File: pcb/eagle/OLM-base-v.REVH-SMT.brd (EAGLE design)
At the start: 91.9 x 57.4 mm, 55 parts, among them CN1 MiniB USB, IC1 LP2985-3.3v, IC2 ATMEGA32U4-AU, IC3 DS1307, IC4 ENC28J60, T1 IRLML2246, U1 USD-SOCKETMICRO-SD-SOCKET-TAO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, X1 8MHz, X2 32.657k, X2A 25MHz, X2A1 25MHz

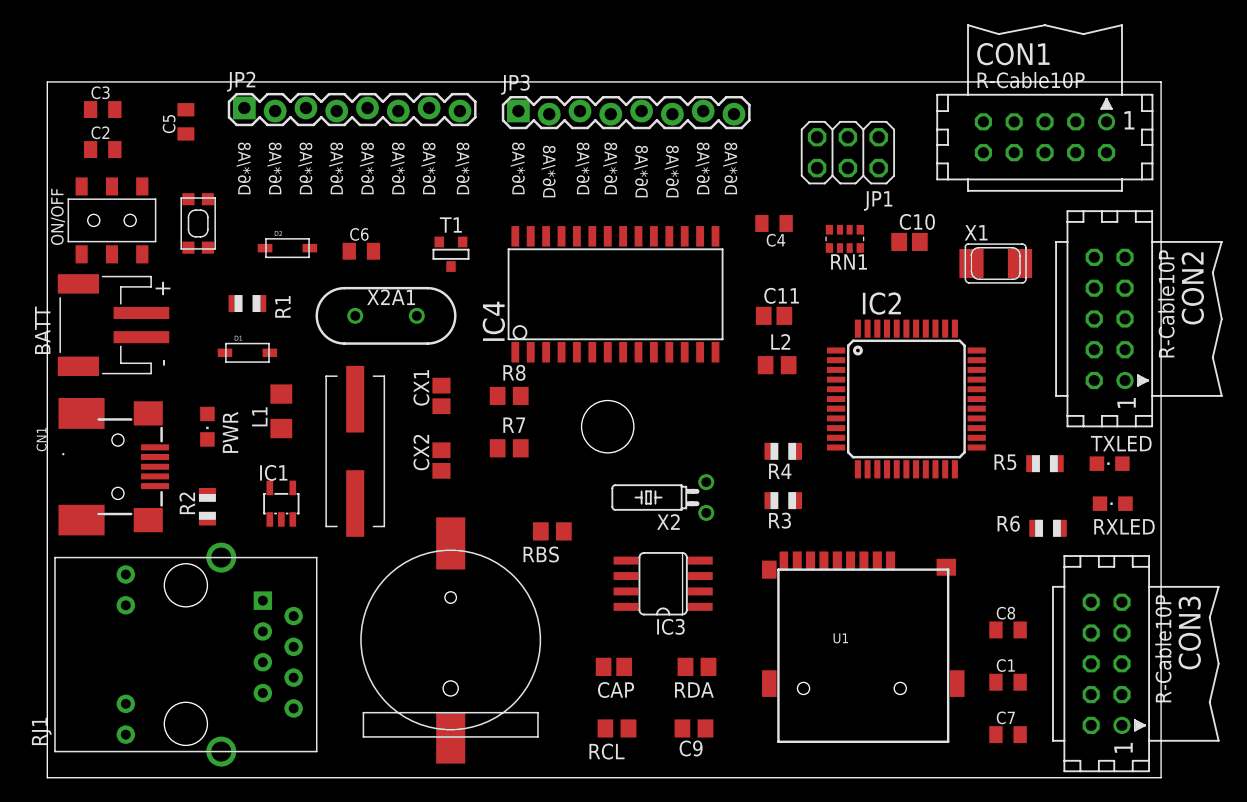
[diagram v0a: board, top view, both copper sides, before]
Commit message: rewired surface mount version
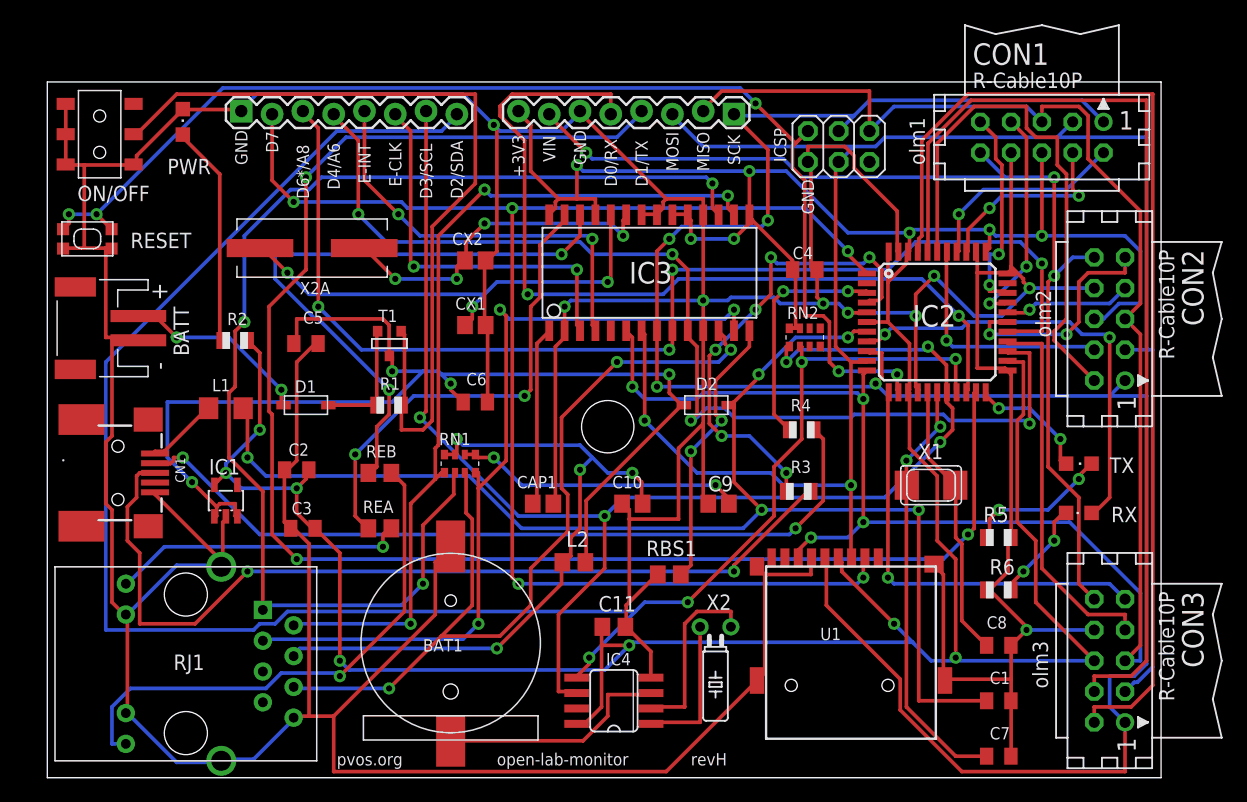
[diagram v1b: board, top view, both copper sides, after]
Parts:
- removed CAP: 10u, resistor:C0805
- removed R7, R8: 330, rcl:R0805
- removed RBS: 2.32K, rcl:R0805
- removed RCL, RDA: 10K, rcl:R0805
- removed RXLED, TXLED: YELLOW, adafruit:CHIPLED_0805
- removed X2A1: 25MHz, SparkFun:HC49US
- added CAP1: 10u, resistor:C0805
- added RBS1: 2.32K, rcl:R0805
- added REA, REB: 330, rcl:R0805
- added RN2: (no value), resistor-dil:EXB38V
- added RX, TX: YELLOW, adafruit:CHIPLED_0805
- C11: value 0.1µ -> 0.1u; device resistor:C0805 -> rcl:C0805
- C9: value 0.1u -> 0.1µ; device rcl:C0805 -> resistor:C0805
- IC3: value DS1307 -> ENC28J60; device adafruit:SO08 -> SparkFun:SOIC28WLONG
- IC4: value ENC28J60 -> DS1307; device SparkFun:SOIC28WLONG -> adafruit:SO08
- X2: value 32.657k -> 32.768kHz
- moved C3 38.3 mm to (21.1, 20.6), turned to 180 degrees
- moved D2 36.9 mm to (54.4, 30.7)
- moved RN1 36.8 mm to (34.0, 25.9), turned to 0 degrees
- moved IC4 33.5 mm to (46.7, 6.35), turned to 90 degrees
- moved C10 31.4 mm to (48.3, 22.6)
- moved C2 30.9 mm to (20.6, 25.4), turned to 180 degrees
- moved C11 28.9 mm to (46.7, 12.4)
- moved IC3 25.7 mm to (50.3, 41.7), turned to 0 degrees
- moved PWR 25.2 mm to (11.2, 54.1), turned to 0 degrees
- moved L2 23.4 mm to (43.4, 17.8)
- moved C5 20.8 mm to (21.3, 35.8), turned to 0 degrees
- moved X1 19.1 mm to (72.9, 24.1)
- moved C9 18.7 mm to (55.4, 22.6)
- moved JP3 17.8 mm to (56.6, 54.9), turned to 180 degrees
- moved X2A 17.1 mm to (21.8, 43.7), turned to 180 degrees
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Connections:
- removed net MISO/D12: CON1.5, CON2.5, CON3.5
- removed net MOSI/D11: CON1.3, CON2.3, CON3.3
- removed net N$34: IC4.27, R7.1
- removed net N$36: BAT1.P$2, IC3.3
- removed net N$37: IC4.26, R8.1
- removed net N$39: CAP.1, IC4.1
- removed net N$41: CX1.1, IC4.24, X2A.P$2, X2A1.2
- removed net N$42: CX2.1, IC4.23, X2A.P$1, X2A1.1
- removed net N$47: IC3.1, X2.1
- removed net N$50: IC3.2, X2.2
- removed net N$54: C10.2, RN1.5, RN1.6
- removed net N$59: IC4.14, RBS.2
- removed net SCK/D13: CON1.1, CON2.1, CON3.1
- new net N$10: C9.2, RN1.5, RN1.6
- new net N$14: IC3.27, REA.1
- new net N$15: IC3.26, REB.1
- new net N$16: CAP1.1, IC3.1
- new net N$17: IC3.14, RBS1.2
- new net N$18: CX1.1, IC3.24, X2A.P$2
- new net N$19: CX2.1, IC3.23, X2A.P$1
- new net N$20: BAT1.P$2, IC4.3
- new net N$21: IC4.1, X2.2
- new net N$30: IC4.2, X2.1
- net +3V3: now also C11.1, IC3.15, IC3.19, IC3.20, IC3.25, IC3.28, IC4.8, JP3.8, RN2.7, RN2.8; no longer C9.1, IC3.8, IC4.15, IC4.19, IC4.20, IC4.25, IC4.28, RCL.1, RDA.1
- net D2/SDA: now also IC4.5, RN2.2; no longer IC3.5, RDA.2
- net D3/SCL: now also IC4.6, RN2.1; no longer IC3.6, RCL.2
- net D4/A6: now also IC3.10; no longer IC4.10
- net D6*/A8: now also IC3.9; no longer IC4.9
- net E-CLK: now also IC3.3; no longer IC4.3
- net E-INT: now also IC3.4; no longer IC4.4
- net GND: now also C11.2, C9.1, CAP1.2, IC3.11, IC3.18, IC3.2, IC3.21, IC3.22, IC4.4, RBS1.1, U1.GND1, U1.GND3, U1.P$1, U1.P$2; no longer C11.1, C9.2, CAP.2, IC3.4, IC4.11, IC4.18, IC4.2, IC4.21, IC4.22, RBS.1
- net LEDA: now also REA.2; no longer R7.2
- net LEDB: now also REB.2; no longer R8.2
- net MISO: now also CON1.5, CON2.5, CON3.5, IC3.6; no longer IC4.6
- net MOSI: now also CON1.3, CON2.3, CON3.3, IC3.7; no longer IC4.7
- net N$11: now also TX.C; no longer TXLED.C
- net N$12: now also RX.C; no longer RXLED.C
- net RD+: now also IC3.13; no longer IC4.13
- net RD-: now also IC3.12; no longer IC4.12
- net RXLED/SS: now also RX.A; no longer RXLED.A
- net SCK: now also CON1.1, CON2.1, CON3.1, IC3.8; no longer IC4.8
- net TCT: now also C10.2; no longer C11.2
- net TD+: now also IC3.17; no longer IC4.17
- net TD-: now also IC3.16; no longer IC4.16
- net TXLED: now also TX.A; no longer TXLED.A
- net VCC: no longer JP3.8
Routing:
- net GND: track 0.00 -> 542.2 mm, vias 0 -> 9
- net +3V3: track 0.00 -> 304.8 mm, vias 0 -> 14
- net SCK: track 0.00 -> 181.6 mm, vias 0 -> 4
- net MISO: track 0.00 -> 163.5 mm, vias 0 -> 4
- net D2/SDA: track 0.00 -> 156.7 mm, vias 0 -> 4
- net MOSI: track 0.00 -> 154.7 mm, vias 0 -> 2
- net D1/TX: track 0.00 -> 132.0 mm, vias 0 -> 3
- net D7/AIN0: track 0.00 -> 119.4 mm, vias 0 -> 5
- net D3/SCL: track 0.00 -> 114.8 mm, vias 0 -> 5
- net +5V: track 0.00 -> 108.5 mm, vias 0 -> 5
- net TD+: track 0.00 -> 100.6 mm, vias 0 -> 3
- net RST: track 0.00 -> 98.6 mm, vias 0 -> 5
- net VCC: track 0.00 -> 95.8 mm, vias 0 -> 4
- net D6*/A8: track 0.00 -> 94.4 mm, vias 0 -> 4
- net D4/A6: track 0.00 -> 88.0 mm, vias 0 -> 4
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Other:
- board text added: "+3V3"
- board text added: "BAT1"
- board text added: "D0/RX"
- board text added: "D1/TX"
- board text added: "D2/SDA"
- board text added: "D3/SCL"
- board text added: "D4/A6"
- board text added: "D7"
- board text added: "E-CLK"
- board text added: "E-INT"
- board text added: "GND"
- board text added: "ICSP"
- board text added: "MISO"
- board text added: "MOSI"
- board text added: "RESET"
- board text added: "SCK"
- board text added: "VIN"
- board text added: "X2A"
- board text added: "olm1"
- board text added: "olm2"
- board text added: "olm3"
- board text added: "open-lab-monitor"
- board text added: "pvos.org"
- board text added: "revH"

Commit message: fixed breakouts by adding reset pin
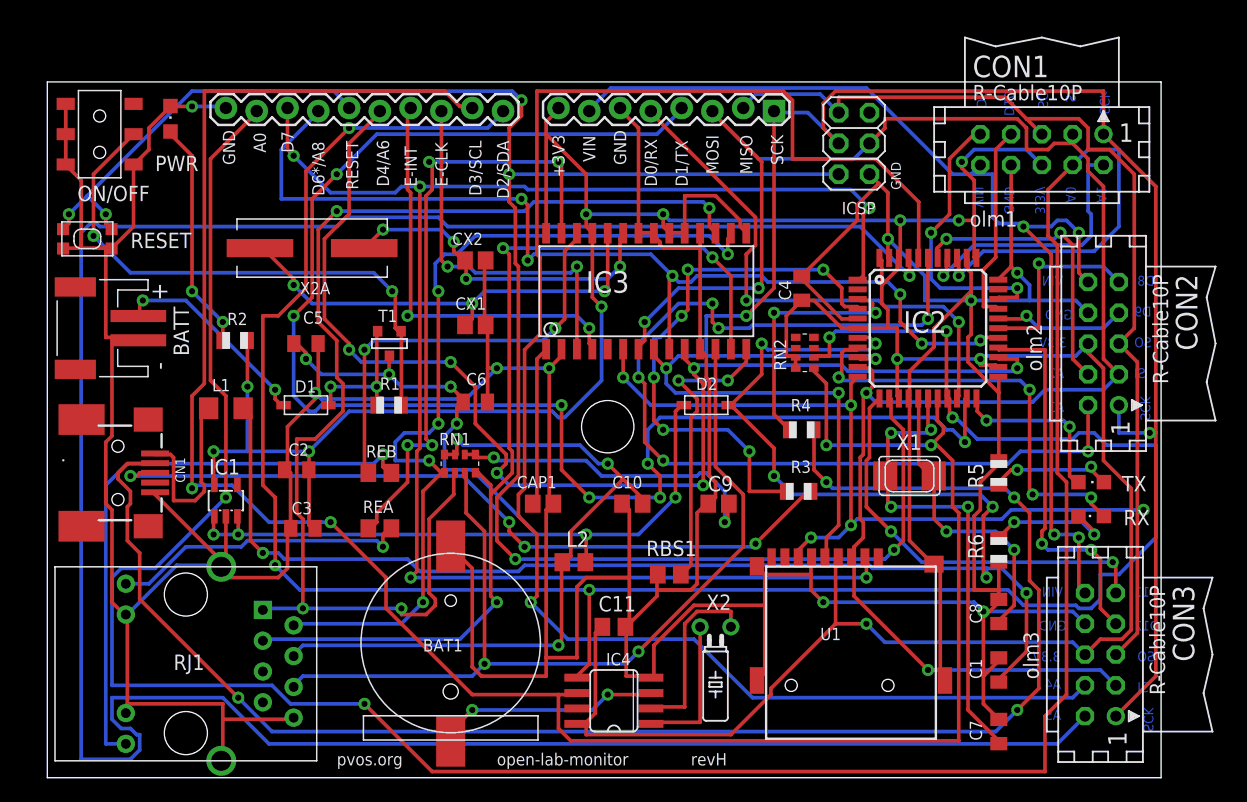
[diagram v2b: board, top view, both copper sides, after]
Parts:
- removed JP2: (no value), SparkFun-Connectors:1X08_LOCK
- added JP4: M10LOCK, SparkFun-Connectors:1X10_LOCK
- moved R5 5.33 mm to (78.5, 25.1), turned to 90 degrees
- moved JP3 3.31 mm to (59.9, 55.1)
- moved R6 3.30 mm to (78.5, 18.8), turned to 90 degrees
- moved C8 2.79 mm to (78.5, 13.7), turned to 90 degrees
- moved C1 2.54 mm to (78.5, 8.89), turned to 90 degrees
- moved CON2 2.09 mm to (87.1, 35.8)
- moved C7 2.03 mm to (78.5, 3.81), turned to 90 degrees
- moved X1 1.93 mm to (71.1, 24.9)
- moved TX 1.83 mm to (86.1, 24.4)
- moved IC3 1.55 mm to (50.0, 40.1)
- moved C4 1.55 mm to (62.2, 40.4), turned to 90 degrees
- moved JP1 1.30 mm to (66.5, 52.3), turned to 270 degrees
- moved RN2 1.27 mm to (62.5, 35.1), turned to 90 degrees
- moved PWR 1.05 mm to (10.2, 54.4)
- moved RX 1.05 mm to (86.1, 21.6)
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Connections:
- net A0: now also JP4.2
- net D2/SDA: now also JP4.10; no longer JP2.8
- net D3/SCL: now also JP4.9; no longer JP2.7
- net D4/A6: now also JP4.6; no longer JP2.4
- net D6*/A8: now also JP4.4; no longer JP2.3
- net D7/AIN0: now also JP4.3; no longer JP2.2
- net E-CLK: now also JP4.8; no longer JP2.6
- net E-INT: now also JP4.7; no longer JP2.5
- net GND: now also JP4.1; no longer JP2.1
- net RST: now also JP4.5
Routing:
- net A0: track 16.0 -> 214.3 mm, vias 2 -> 3
- net A5: track 85.6 -> 209.8 mm, vias 0 -> 1
- net N$5: track 65.5 -> 132.3 mm, vias 2 -> 4
- net D3/SCL: track 114.8 -> 178.1 mm, vias 5 -> 4
- net RST: track 98.6 -> 160.8 mm, vias 5 -> 6
- net A4: track 80.8 -> 136.0 mm, vias 0 -> 1
- net A3: track 44.4 -> 82.2 mm, vias 0 -> 6
- net GND: track 542.2 -> 508.0 mm
- net +5V: track 108.5 -> 137.0 mm, vias 5 -> 7
- net D2/SDA: track 156.7 -> 184.8 mm, vias 4 -> 6
- net D0/RX: track 71.7 -> 44.1 mm
- net N$13: track 69.2 -> 46.2 mm, vias 0 -> 2
- net MISO: track 163.5 -> 147.2 mm, vias 4 -> 5
- net N$15: track 50.4 -> 35.4 mm
- net D4/A6: track 88.0 -> 101.4 mm, vias 4 -> 6
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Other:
- board text added: "3.3V"
- board text added: "A0"
- board text added: "A1"
- board text added: "A2"
- board text added: "A3"
- board text added: "A4"
- board text added: "A5"
- board text added: "D10"
- board text added: "D11"
- board text added: "D12"
- board text added: "D5"
- board text added: "D8"
- board text added: "D9"
- board text added: "SCk"
- board text added: "SI"
- board text added: "SO"

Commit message: removed pin labels on bottom of board to satisfy seeed design rules
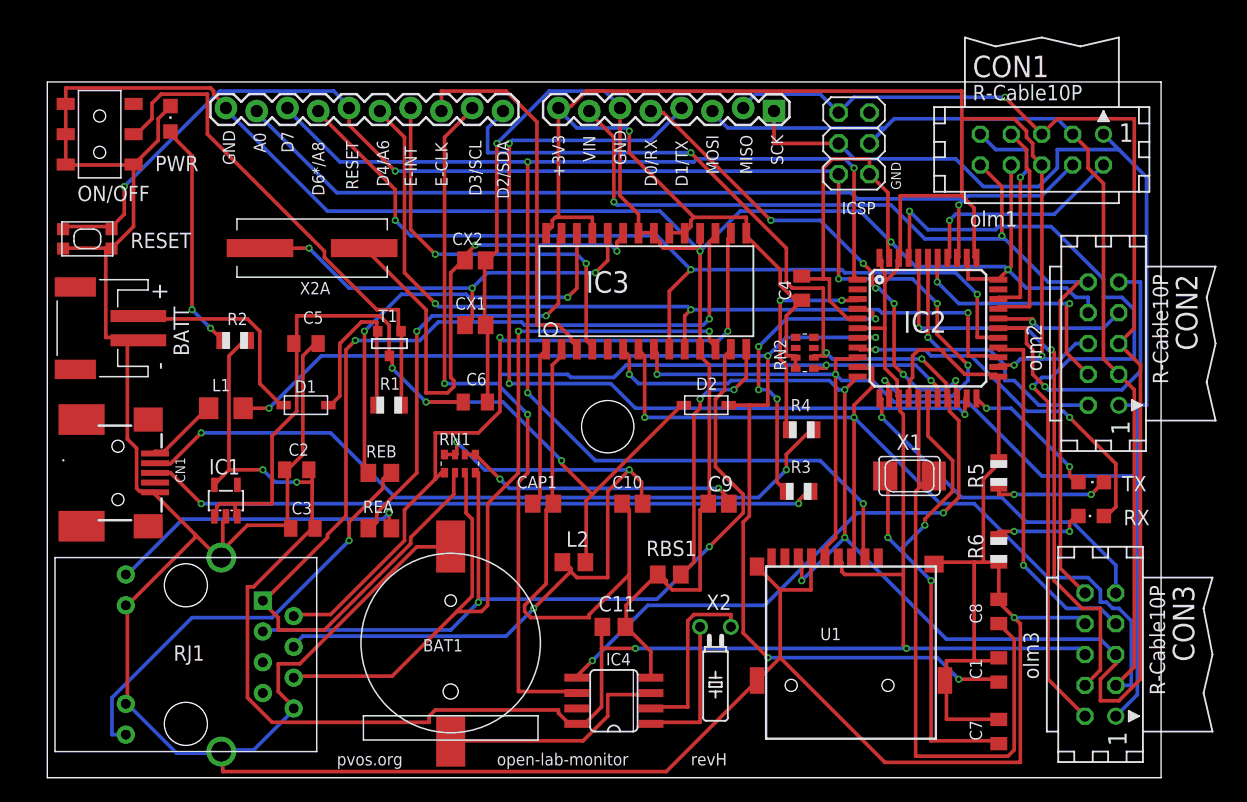
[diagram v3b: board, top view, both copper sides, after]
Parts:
- moved RJ1 0.76 mm to (11.4, 10.2)
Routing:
- net A5: track 209.8 -> 69.3 mm, vias 1 -> 2
- net A0: track 214.3 -> 76.7 mm, vias 3 -> 1
- net A4: track 136.0 -> 48.3 mm, vias 1 -> 2
- net GND: track 508.0 -> 592.7 mm, vias 9 -> 5
- net D2/SDA: track 184.8 -> 103.5 mm, vias 6 -> 5
- net D3/SCL: track 178.1 -> 100.1 mm
- net N$5: track 132.3 -> 60.7 mm, vias 4 -> 2
- net A3: track 82.2 -> 22.8 mm, vias 6 -> 1
- net RST: track 160.8 -> 108.6 mm
- net D1/TX: track 124.9 -> 75.4 mm, vias 7 -> 3
- net +5V: track 137.0 -> 105.3 mm, vias 7 -> 5
- net D4/A6: track 101.4 -> 71.6 mm, vias 6 -> 3
- net N$9: track 24.9 -> 50.6 mm, vias 2 -> 0
- net N$4: track 45.4 -> 25.9 mm, vias 6 -> 4
- net +3V3: track 292.3 -> 311.5 mm, vias 12 -> 7
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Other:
- board text removed: "3.3V"
- board text removed: "A1"
- board text removed: "A2"
- board text removed: "A3"
- board text removed: "A4"
- board text removed: "A5"
- board text removed: "D10"
- board text removed: "D11"
- board text removed: "D12"
- board text removed: "D5"
- board text removed: "D8"
- board text removed: "D9"
- board text removed: "SCk"
- board text removed: "SI"
- board text removed: "SO"
